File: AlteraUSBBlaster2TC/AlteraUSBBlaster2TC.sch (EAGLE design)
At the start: 13 parts, among them U1 NCP1117LPST33T3G

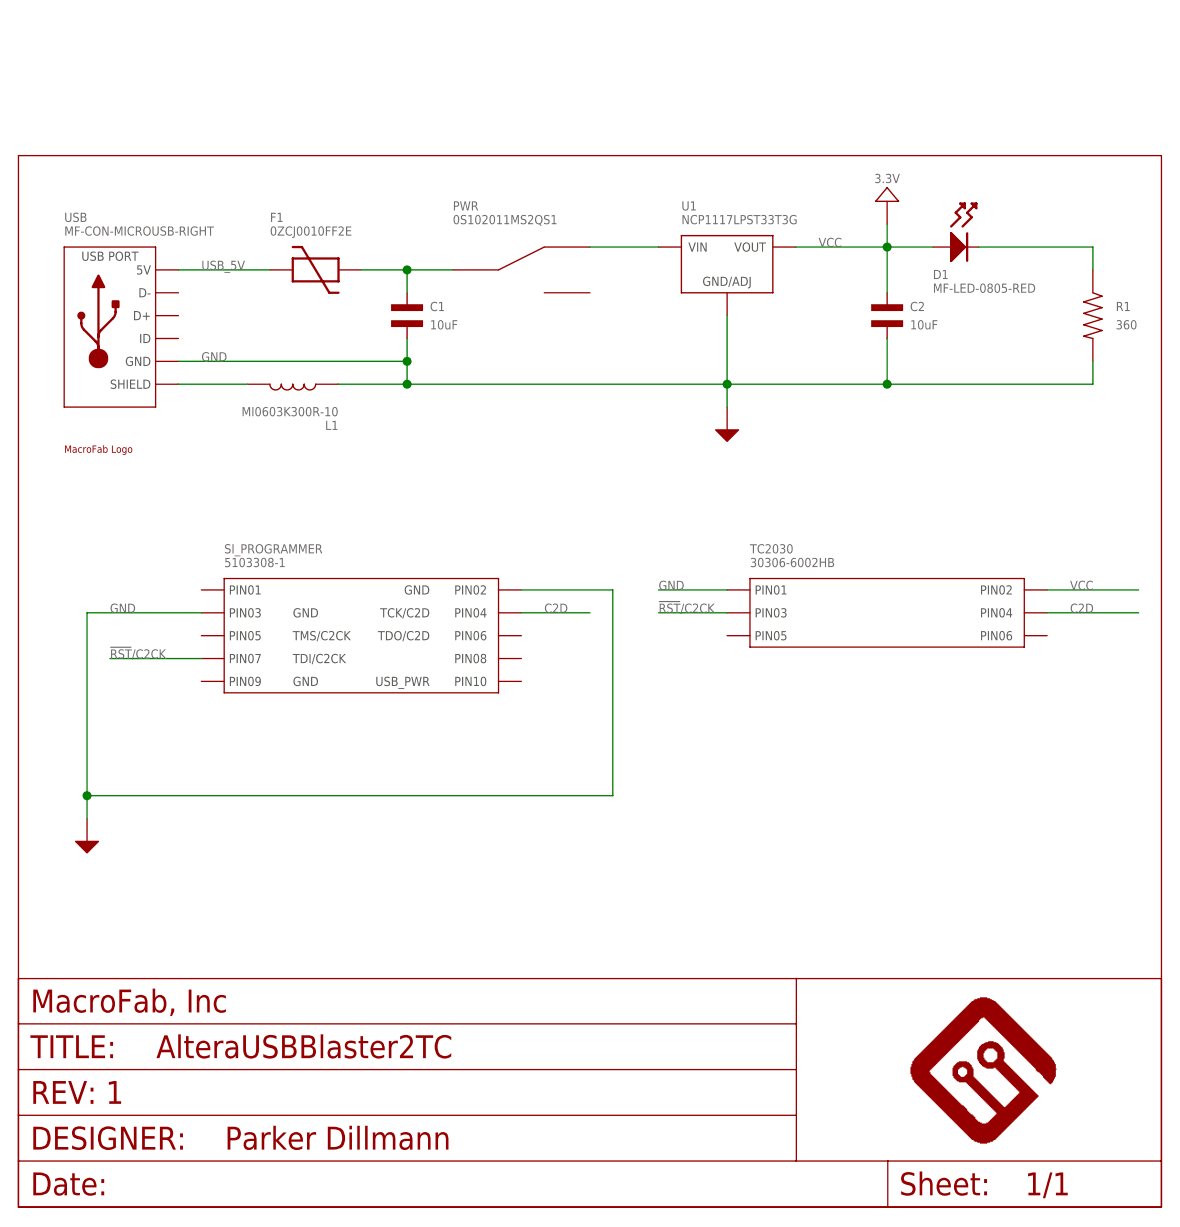
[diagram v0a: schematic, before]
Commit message: Added AVRISP2TC
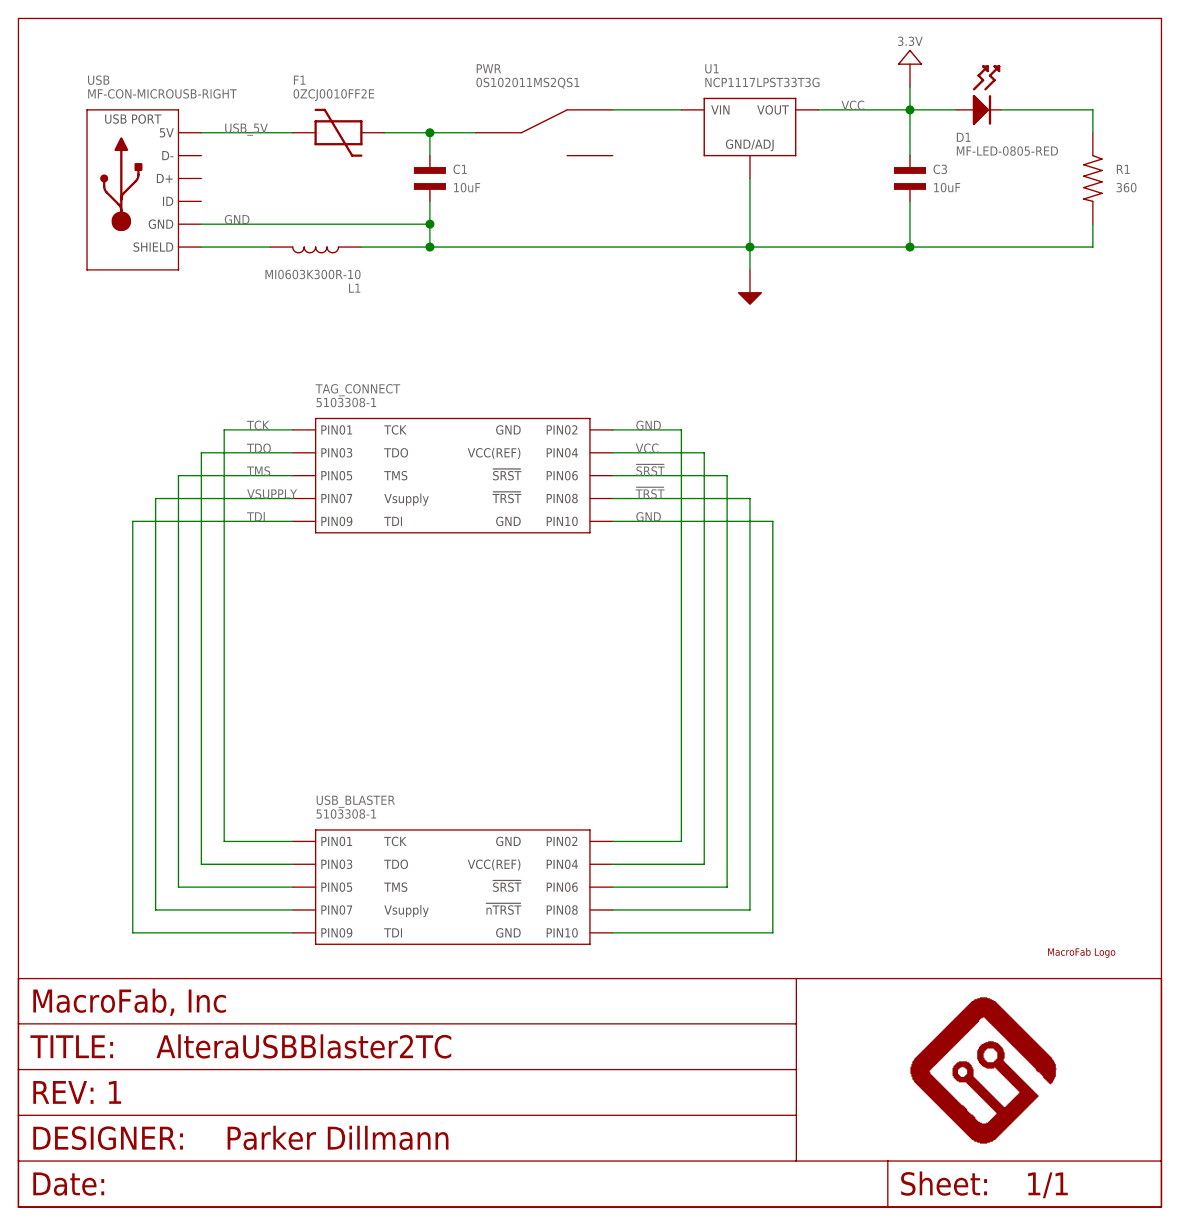
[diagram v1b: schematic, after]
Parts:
- removed C2: 10uF, MF_Passives:CAPACITOR_NP_1206
- removed SI_PROGRAMMER: 5103308-1, PP_Connectors:CON_02X05_5103308-1
- removed TC2030: 30306-6002HB, PP_Connectors:CON_02X03_30306-6002HB
- added C3: 10uF, MF_Passives:CAPACITOR_NP_1206
- added TAG_CONNECT, USB_BLASTER: 5103308-1, PP_Connectors:CON_02X05_5103308-1
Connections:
- removed net !RST!/C2CK: SI_PROGRAMMER.PIN7, TC2030.PIN3
- removed net C2D: SI_PROGRAMMER.PIN4, TC2030.PIN4
- new net !SRST: TAG_CONNECT.PIN6, USB_BLASTER.PIN6
- new net !TRST: TAG_CONNECT.PIN8, USB_BLASTER.PIN8
- new net TCK: TAG_CONNECT.PIN1, USB_BLASTER.PIN1
- new net TDI: TAG_CONNECT.PIN9, USB_BLASTER.PIN9
- new net TDO: TAG_CONNECT.PIN3, USB_BLASTER.PIN3
- new net TMS: TAG_CONNECT.PIN5, USB_BLASTER.PIN5
- new net VSUPPLY: TAG_CONNECT.PIN7, USB_BLASTER.PIN7
- net GND: now also C3.P$2, TAG_CONNECT.PIN10, TAG_CONNECT.PIN2, USB_BLASTER.PIN10, USB_BLASTER.PIN2; no longer C2.P$2, SI_PROGRAMMER.PIN2, SI_PROGRAMMER.PIN3, TC2030.PIN1
- net VCC: now also C3.P$1, TAG_CONNECT.PIN4, USB_BLASTER.PIN4; no longer C2.P$1, TC2030.PIN2
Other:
- moved on the sheet: C1, D1, F1, L1, PWR, R1, U1, USB
